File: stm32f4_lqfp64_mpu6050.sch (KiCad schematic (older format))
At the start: 0 parts

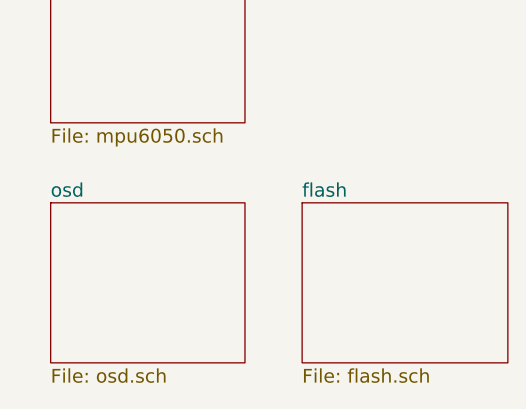
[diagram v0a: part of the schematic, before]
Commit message: routing finished - essential signals only
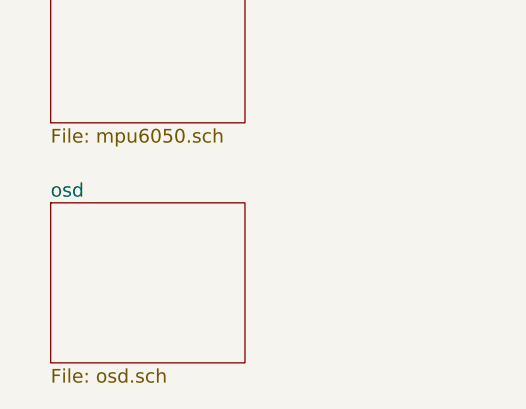
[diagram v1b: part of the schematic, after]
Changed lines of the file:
@@
 $Descr A4 11693 8268
 encoding utf-8
-Sheet 1 8
+Sheet 1 7
 Title ""
 Date ""
@@
 F1 "motors.sch" 60
 $EndSheet
-$Sheet
-S 3900 1750 900  700
-U 5729526E
-F0 "flash" 60
-F1 "flash.sch" 60
-$EndSheet
 $EndSCHEMATC
